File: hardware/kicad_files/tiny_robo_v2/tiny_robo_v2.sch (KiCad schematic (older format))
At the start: 31 parts, among them P2 BATT, P3 CONN_01X02, P4 CONNECTOR, P5 CONNECTOR, P6 CONN_01X02, SW1 SPDT, U1 MCP73831, U2 MIC5265, U3 ESP8266-ESP-03, U4 DRV8830, U5 DRV8830

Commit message: Fixed switch footprint, working on PCB now
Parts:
- Charge1: footprint LEDs:LED-0805 -> LEDs:LED_0805
- P1: renamed from P?; footprint (none) -> Pin_Headers:Pin_Header_Straight_1x06
- R10, R11, R12: renamed from R?; footprint (none) -> Resistors_SMD:R_1206_HandSoldering
- U1, U2: footprint Housings_SOT-23_SOT-143_TSOT-6:SOT-23-5 -> TO_SOT_Packages_SMD:SOT-23-5
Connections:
- net 5Vin: now also P1.4 (P4)
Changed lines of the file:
@@
 $EndComp
 $Comp
-L +3.3V-RESCUE-tiny_robo_v2 #PWR05
+L +3.3V-RESCUE-tiny_robo_v2 #PWR04
 U 1 1 5575F5D2
 P 4500 4800
-F 0 "#PWR05" H 4500 4760 30  0001 C CNN
+F 0 "#PWR04" H 4500 4760 30  0001 C CNN
 F 1 "+3.3V" H 4500 4910 30  0000 C CNN
 F 2 "" H 4500 4800 60  0001 C CNN
@@
 NoConn ~ 7800 1900
 $Comp
-L +BATT #PWR06
+L +BATT #PWR05
 U 1 1 54EFA680
 P 5650 975
-F 0 "#PWR06" H 5650 925 20  0001 C CNN
+F 0 "#PWR05" H 5650 925 20  0001 C CNN
 F 1 "+BATT" H 5650 1075 30  0000 C CNN
 F 2 "" H 5650 975 60  0001 C CNN
@@
 $EndComp
 $Comp
-L +3.3V-RESCUE-tiny_robo_v2 #PWR07
+L +3.3V-RESCUE-tiny_robo_v2 #PWR06
 U 1 1 54EFA66A
 P 8550 1325
-F 0 "#PWR07" H 8550 1285 30  0001 C CNN
+F 0 "#PWR06" H 8550 1285 30  0001 C CNN
 F 1 "+3.3V" H 8550 1435 30  0000 C CNN
 F 2 "" H 8550 1325 60  0001 C CNN
@@
 F 0 "U2" H 7350 2000 60  0000 C CNN
 F 1 "MIC5265" H 7500 1600 60  0000 C CNN
-F 2 "Housings_SOT-23_SOT-143_TSOT-6:SOT-23-5" H 7500 1800 60  0000 C CNN
+F 2 "TO_SOT_Packages_SMD:SOT-23-5" H 7500 1800 60  0000 C CNN
 F 3 "~" H 7500 1800 60  0000 C CNN
 	1    7500 1800
@@
 F 0 "U1" H 4700 2150 60  0000 C CNN
 F 1 "MCP73831" H 4850 1750 60  0000 C CNN
-F 2 "Housings_SOT-23_SOT-143_TSOT-6:SOT-23-5" H 4850 1950 60  0000 C CNN
+F 2 "TO_SOT_Packages_SMD:SOT-23-5" H 4850 1950 60  0000 C CNN
 F 3 "~" H 4850 1950 60  0000 C CNN
 	1    4850 1950
@@
 F 0 "Charge1" H 3650 2150 50  0000 C CNN
 F 1 "LED" H 3650 1950 50  0000 C CNN
-F 2 "LEDs:LED-0805" H 3650 2050 60  0001 C CNN
+F 2 "LEDs:LED_0805" H 3650 2050 60  0001 C CNN
 F 3 "" H 3650 2050 60  0001 C CNN
 	1    3650 2050
@@
 $EndComp
 $Comp
-L GND-RESCUE-tiny_robo_v2 #PWR08
+L GND-RESCUE-tiny_robo_v2 #PWR07
 U 1 1 54EF9ED1
 P 4450 2700
-F 0 "#PWR08" H 4450 2700 30  0001 C CNN
+F 0 "#PWR07" H 4450 2700 30  0001 C CNN
 F 1 "GND" H 4450 2630 30  0001 C CNN
 F 2 "" H 4450 2700 60  0001 C CNN
@@
 	2975 3225 2975 3725
 $Comp
-L GND-RESCUE-tiny_robo_v2 #PWR09
+L GND-RESCUE-tiny_robo_v2 #PWR08
 U 1 1 559D6D0E
 P 2975 3725
-F 0 "#PWR09" H 2975 3725 30  0001 C CNN
+F 0 "#PWR08" H 2975 3725 30  0001 C CNN
 F 1 "GND" H 2975 3655 30  0001 C CNN
 F 2 "" H 2975 3725 60  0000 C CNN
@@
 $EndComp
 $Comp
-L CONN_01X06 P?
+L CONN_01X06 P1
 U 1 1 570E7DDF
 P 2775 5050
-F 0 "P?" H 2775 5400 50  0000 C CNN
+F 0 "P1" H 2775 5400 50  0000 C CNN
 F 1 "CONN_01X06" V 2875 5050 50  0000 C CNN
-F 2 "" H 2775 5050 50  0000 C CNN
+F 2 "Pin_Headers:Pin_Header_Straight_1x06" H 2775 5050 50  0001 C CNN
 F 3 "" H 2775 5050 50  0000 C CNN
 	1    2775 5050
@@
 	3125 4900 2975 4900
 $Comp
-L GND-RESCUE-tiny_robo_v2 #PWR?
+L GND-RESCUE-tiny_robo_v2 #PWR09
 U 1 1 570E86D9
 P 3700 4850
-F 0 "#PWR?" H 3700 4850 30  0001 C CNN
+F 0 "#PWR09" H 3700 4850 30  0001 C CNN
 F 1 "GND-RESCUE-tiny_robo_v2" H 3700 4780 30  0001 C CNN
 F 2 "" H 3700 4850 60  0000 C CNN
@@
 Connection ~ 3700 4800
 $Comp
-L R-RESCUE-tiny_robo_v2 R?
+L R-RESCUE-tiny_robo_v2 R11
 U 1 1 570E8A3E
 P 5125 4425
-F 0 "R?" V 5205 4425 40  0000 C CNN
+F 0 "R11" V 5205 4425 40  0000 C CNN
 F 1 "10k" V 5132 4426 40  0000 C CNN
-F 2 "" V 5055 4425 30  0000 C CNN
+F 2 "Resistors_SMD:R_1206_HandSoldering" V 5055 4425 30  0001 C CNN
 F 3 "" H 5125 4425 30  0000 C CNN
 	1    5125 4425
@@
 $EndComp
 $Comp
-L R-RESCUE-tiny_robo_v2 R?
+L R-RESCUE-tiny_robo_v2 R12
 U 1 1 570E8B63
 P 6125 4475
-F 0 "R?" V 6205 4475 40  0000 C CNN
+F 0 "R12" V 6205 4475 40  0000 C CNN
 F 1 "10k" V 6132 4476 40  0000 C CNN
-F 2 "" V 6055 4475 30  0000 C CNN
+F 2 "Resistors_SMD:R_1206_HandSoldering" V 6055 4475 30  0001 C CNN
 F 3 "" H 6125 4475 30  0000 C CNN
 	1    6125 4475
@@
 	3700 4225 6125 4225
 $Comp
-L R-RESCUE-tiny_robo_v2 R?
+L R-RESCUE-tiny_robo_v2 R10
 U 1 1 57156590
 P 3250 4425
-F 0 "R?" V 3330 4425 40  0000 C CNN
+F 0 "R10" V 3330 4425 40  0000 C CNN
 F 1 "10k" V 3257 4426 40  0000 C CNN
-F 2 "" V 3180 4425 30  0000 C CNN
+F 2 "Resistors_SMD:R_1206_HandSoldering" V 3180 4425 30  0001 C CNN
 F 3 "" H 3250 4425 30  0000 C CNN
 	1    3250 4425
@@
 Wire Wire Line
 	4325 4800 4575 4800
+Wire Wire Line
+	2975 4125 2975 5000
+Text GLabel 2400 4125 0    60   Input ~ 0
+5Vin
+Wire Wire Line
+	2975 4125 2400 4125
 $EndSCHEMATC

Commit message: syncing home version
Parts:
- added C? (x2): 0.1uF, Capacitors_SMD:C_0805_HandSoldering, symbol C-RESCUE-tiny_robo_v2
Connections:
- net GND: now also C?.2, C?.2
- net Unreg: now also C?.1, C?.1
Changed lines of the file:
@@
 EESchema Schematic File Version 2
+LIBS:tiny_robo_v2-rescue
 LIBS:power
 LIBS:device
@@
 	5650 1300 6275 1300
 Wire Wire Line
-	8650 5525 8650 6600
+	8650 5450 8650 6600
 Connection ~ 7850 6600
 Connection ~ 9650 3775
@@
 Wire Wire Line
 	2975 4125 2400 4125
+$Comp
+L C-RESCUE-tiny_robo_v2 C?
+U 1 1 57E440DA
+P 8975 5450
+F 0 "C?" H 9025 5550 50  0000 L CNN
+F 1 "0.1uF" H 9025 5350 50  0000 L CNN
+F 2 "Capacitors_SMD:C_0805_HandSoldering" H 8975 5450 60  0001 C CNN
+F 3 "" H 8975 5450 60  0001 C CNN
+	1    8975 5450
+	0    1    1    0
+$EndComp
+$Comp
+L C-RESCUE-tiny_robo_v2 C?
+U 1 1 57E442F8
+P 8975 5750
+F 0 "C?" H 9025 5850 50  0000 L CNN
+F 1 "0.1uF" H 9025 5650 50  0000 L CNN
+F 2 "Capacitors_SMD:C_0805_HandSoldering" H 8975 5750 60  0001 C CNN
+F 3 "" H 8975 5750 60  0001 C CNN
+	1    8975 5750
+	0    1    1    0
+$EndComp
+Wire Wire Line
+	8775 5450 8650 5450
+Connection ~ 8650 5525
+Wire Wire Line
+	8775 5750 8650 5750
+Connection ~ 8650 5750
+Wire Wire Line
+	8375 6225 8375 6175
+Wire Wire Line
+	8375 6175 8825 6175
+Wire Wire Line
+	8825 6175 8825 5850
+Wire Wire Line
+	8825 5850 9175 5850
+Wire Wire Line
+	9175 5850 9175 5750
+Wire Wire Line
+	8375 5200 8375 5250
+Wire Wire Line
+	8375 5250 9000 5250
+Wire Wire Line
+	9000 5250 9000 5400
+Wire Wire Line
+	9000 5400 9175 5400
+Wire Wire Line
+	9175 5400 9175 5450
 $EndSCHEMATC

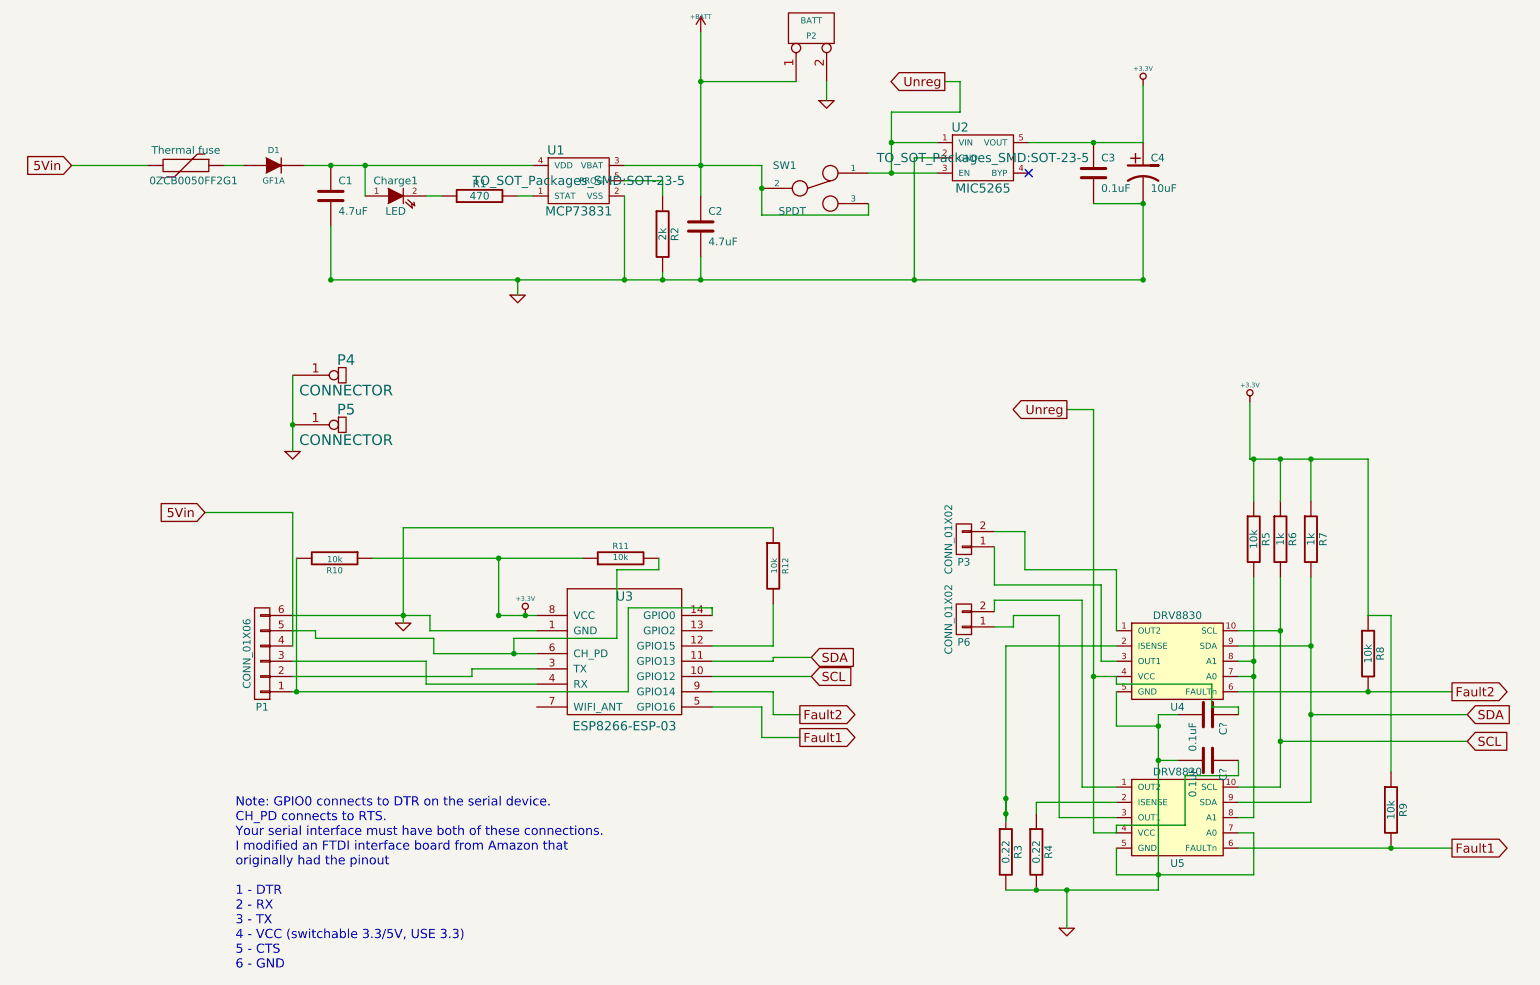
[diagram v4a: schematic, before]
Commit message: Updated schematic, board probably needs relayout (after I graduate).
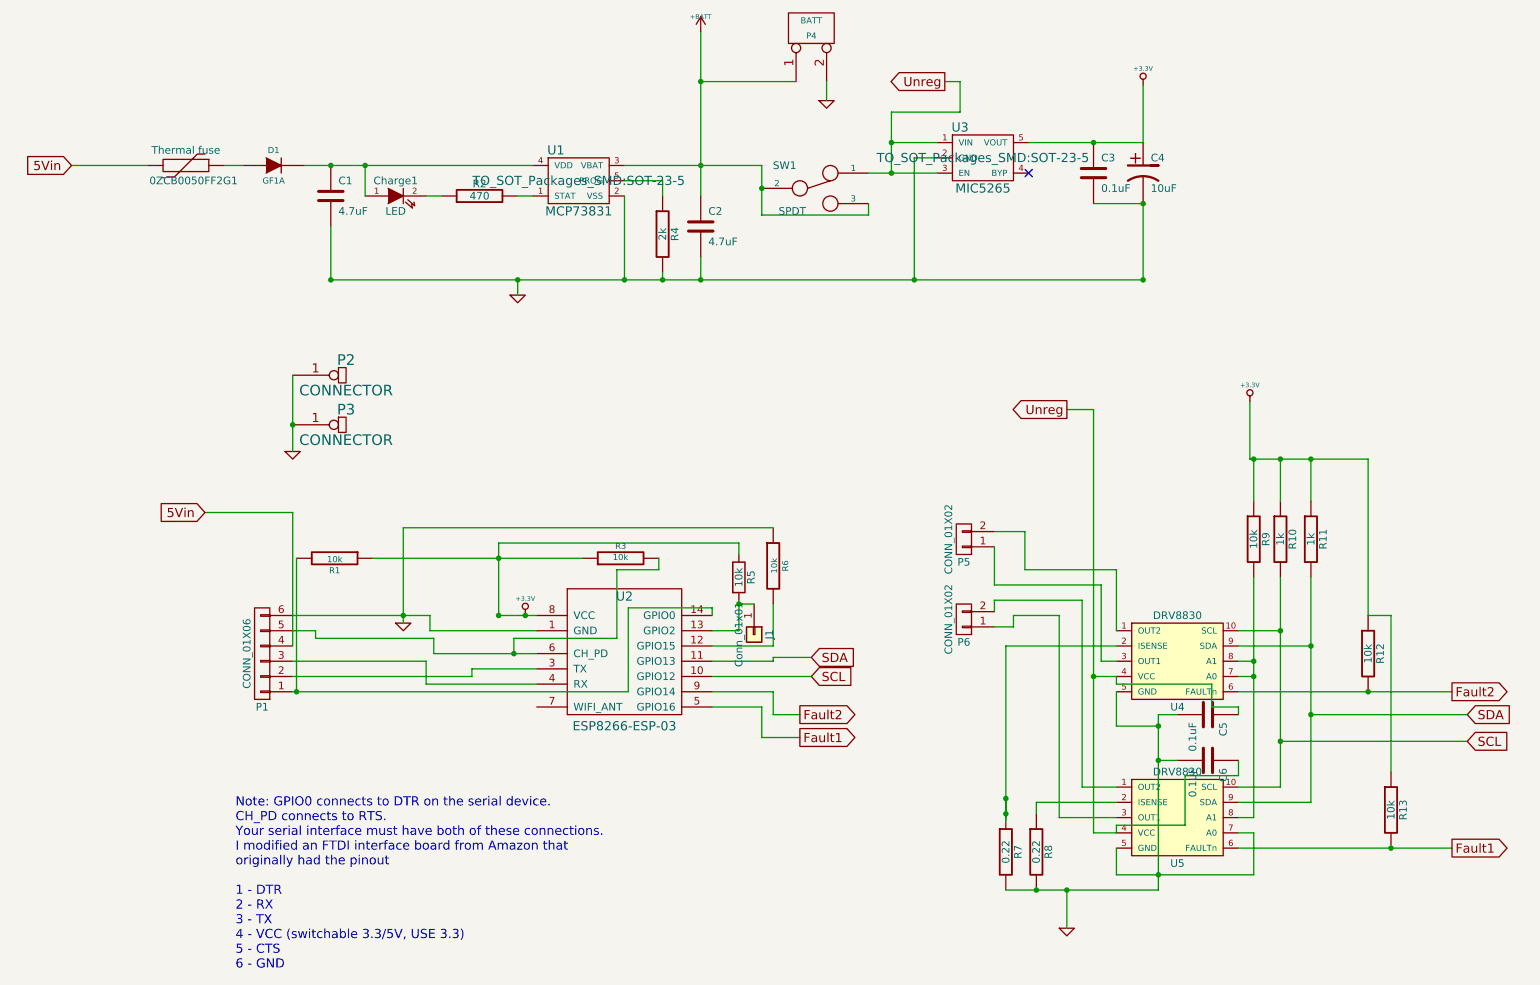
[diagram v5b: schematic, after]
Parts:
- added J1: Conn_01x01, Pin_Headers:Pin_Header_Straight_1x01_Pitch1.00mm, symbol Conn_01x01
- added R5: 10k, Resistors_SMD:R_1206_HandSoldering, symbol R
- gave numbers to parts that had none: 2
- renumbered P4 to P2, P5 to P3, P2 to P4, P3 to P5, R10 to R1, R6 to R10, R7 to R11, R8 to R12, R9 to R13, R1 to R2, R11 to R3, R2 to R4, R12 to R6, R3 to R7, R4 to R8, R5 to R9, U3 to U2, U2 to U3
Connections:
- net +3.3V: now also R5.1
- net at U2.13 (GPIO2): now also J1.1 (Pin_1), R5.2
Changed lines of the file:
@@
 EESchema Schematic File Version 2
-LIBS:tiny_robo_v2-rescue
 LIBS:power
 LIBS:device
@@
 $EndComp
 $Comp
-L R-RESCUE-tiny_robo_v2 R5
+L R-RESCUE-tiny_robo_v2 R9
 U 1 1 5576FFFF
 P 9275 4300
-F 0 "R5" V 9355 4300 50  0000 C CNN
+F 0 "R9" V 9355 4300 50  0000 C CNN
 F 1 "10k" V 9275 4300 50  0000 C CNN
 F 2 "Resistors_SMD:R_1206_HandSoldering" H 9275 4300 60  0001 C CNN
@@
 $EndComp
 $Comp
-L R-RESCUE-tiny_robo_v2 R8
+L R-RESCUE-tiny_robo_v2 R12
 U 1 1 5576FE5F
 P 10025 5050
-F 0 "R8" V 10105 5050 50  0000 C CNN
+F 0 "R12" V 10105 5050 50  0000 C CNN
 F 1 "10k" V 10025 5050 50  0000 C CNN
 F 2 "Resistors_SMD:R_1206_HandSoldering" H 10025 5050 60  0001 C CNN
@@
 $EndComp
 $Comp
-L R-RESCUE-tiny_robo_v2 R9
+L R-RESCUE-tiny_robo_v2 R13
 U 1 1 5576FE58
 P 10175 6075
-F 0 "R9" V 10255 6075 50  0000 C CNN
+F 0 "R13" V 10255 6075 50  0000 C CNN
 F 1 "10k" V 10175 6075 50  0000 C CNN
 F 2 "Resistors_SMD:R_1206_HandSoldering" H 10175 6075 60  0001 C CNN
@@
 $EndComp
 $Comp
-L R-RESCUE-tiny_robo_v2 R7
+L R-RESCUE-tiny_robo_v2 R11
 U 1 1 5576FE2F
 P 9650 4300
-F 0 "R7" V 9730 4300 50  0000 C CNN
+F 0 "R11" V 9730 4300 50  0000 C CNN
 F 1 "1k" V 9650 4300 50  0000 C CNN
 F 2 "Resistors_SMD:R_1206_HandSoldering" H 9650 4300 60  0001 C CNN
@@
 $EndComp
 $Comp
-L R-RESCUE-tiny_robo_v2 R6
+L R-RESCUE-tiny_robo_v2 R10
 U 1 1 5576FE2B
 P 9450 4300
-F 0 "R6" V 9530 4300 50  0000 C CNN
+F 0 "R10" V 9530 4300 50  0000 C CNN
 F 1 "1k" V 9450 4300 50  0000 C CNN
 F 2 "Resistors_SMD:R_1206_HandSoldering" H 9450 4300 60  0001 C CNN
@@
 $EndComp
 $Comp
-L R-RESCUE-tiny_robo_v2 R4
+L R-RESCUE-tiny_robo_v2 R8
 U 1 1 5576FE28
 P 7850 6350
-F 0 "R4" V 7930 6350 50  0000 C CNN
+F 0 "R8" V 7930 6350 50  0000 C CNN
 F 1 "0.22" V 7850 6350 50  0000 C CNN
 F 2 "Resistors_SMD:R_1206_HandSoldering" H 7850 6350 60  0001 C CNN
@@
 $EndComp
 $Comp
-L R-RESCUE-tiny_robo_v2 R3
+L R-RESCUE-tiny_robo_v2 R7
 U 1 1 5576FE1B
 P 7650 6350
-F 0 "R3" V 7730 6350 50  0000 C CNN
+F 0 "R7" V 7730 6350 50  0000 C CNN
 F 1 "0.22" V 7650 6350 50  0000 C CNN
 F 2 "Resistors_SMD:R_1206_HandSoldering" H 7650 6350 60  0001 C CNN
@@
 $EndComp
 $Comp
-L CONN_2 P2
+L CONN_2 P4
 U 1 1 54EFA433
 P 6375 950
-F 0 "P2" V 6325 950 40  0000 C CNN
+F 0 "P4" V 6325 950 40  0000 C CNN
 F 1 "BATT" V 6425 950 40  0000 C CNN
 F 2 "Pin_Headers:Pin_Header_Straight_1x02" H 6375 950 60  0001 C CNN
@@
 $EndComp
 $Comp
-L MIC5265 U2
+L MIC5265 U3
 U 1 1 54EFA34D
 P 7500 1800
-F 0 "U2" H 7350 2000 60  0000 C CNN
+F 0 "U3" H 7350 2000 60  0000 C CNN
 F 1 "MIC5265" H 7500 1600 60  0000 C CNN
 F 2 "TO_SOT_Packages_SMD:SOT-23-5" H 7500 1800 60  0000 C CNN
@@
 $EndComp
 $Comp
-L R-RESCUE-tiny_robo_v2 R1
+L R-RESCUE-tiny_robo_v2 R2
 U 1 1 54EF9F5C
 P 4200 2050
-F 0 "R1" V 4280 2050 50  0000 C CNN
+F 0 "R2" V 4280 2050 50  0000 C CNN
 F 1 "470" V 4200 2050 50  0000 C CNN
 F 2 "Resistors_SMD:R_1206_HandSoldering" H 4200 2050 60  0001 C CNN
@@
 $EndComp
 $Comp
-L R-RESCUE-tiny_robo_v2 R2
+L R-RESCUE-tiny_robo_v2 R4
 U 1 1 54EF9F56
 P 5400 2300
-F 0 "R2" V 5480 2300 50  0000 C CNN
+F 0 "R4" V 5480 2300 50  0000 C CNN
 F 1 "2k" V 5400 2300 50  0000 C CNN
 F 2 "Resistors_SMD:R_1206_HandSoldering" H 5400 2300 60  0001 C CNN
@@
 	9175 5300 10575 5300
 $Comp
-L CONNECTOR P4
+L CONNECTOR P2
 U 1 1 559D6607
 P 2975 3225
-F 0 "P4" H 3325 3325 70  0000 C CNN
+F 0 "P2" H 3325 3325 70  0000 C CNN
 F 1 "CONNECTOR" H 3325 3125 70  0000 C CNN
 F 2 "Wire_Pads:SolderWirePad_single_0-8mmDrill" H 2975 3225 60  0001 C CNN
@@
 $EndComp
 $Comp
-L CONNECTOR P5
+L CONNECTOR P3
 U 1 1 559D66C8
 P 2975 3550
-F 0 "P5" H 3325 3650 70  0000 C CNN
+F 0 "P3" H 3325 3650 70  0000 C CNN
 F 1 "CONNECTOR" H 3325 3450 70  0000 C CNN
 F 2 "Wire_Pads:SolderWirePad_single_0-8mmDrill" H 2975 3550 60  0001 C CNN
@@
 Connection ~ 2975 3550
 $Comp
-L CONN_01X02 P3
+L CONN_01X02 P5
 U 1 1 559D733F
 P 7375 4300
-F 0 "P3" H 7375 4450 50  0000 C CNN
+F 0 "P5" H 7375 4450 50  0000 C CNN
 F 1 "CONN_01X02" V 7475 4300 50  0000 C CNN
 F 2 "Pin_Headers:Pin_Header_Straight_1x02" H 7375 4300 60  0001 C CNN
@@
 	6050 5600 6300 5600
 $Comp
-L ESP8266-ESP-03 U3
+L ESP8266-ESP-03 U2
 U 1 1 5575F418
 P 5150 5400
-F 0 "U3" H 5150 6125 60  0000 C CNN
+F 0 "U2" H 5150 6125 60  0000 C CNN
 F 1 "ESP8266-ESP-03" H 5150 5275 60  0000 C CNN
 F 2 "esp-8266:ESP8266-ESP-03" H 5150 5400 60  0001 C CNN
@@
 Connection ~ 3700 4800
 $Comp
-L R-RESCUE-tiny_robo_v2 R11
+L R-RESCUE-tiny_robo_v2 R3
 U 1 1 570E8A3E
 P 5125 4425
-F 0 "R11" V 5205 4425 40  0000 C CNN
+F 0 "R3" V 5205 4425 40  0000 C CNN
 F 1 "10k" V 5132 4426 40  0000 C CNN
 F 2 "Resistors_SMD:R_1206_HandSoldering" V 5055 4425 30  0001 C CNN
@@
 $EndComp
 $Comp
-L R-RESCUE-tiny_robo_v2 R12
+L R-RESCUE-tiny_robo_v2 R6
 U 1 1 570E8B63
 P 6125 4475
-F 0 "R12" V 6205 4475 40  0000 C CNN
+F 0 "R6" V 6205 4475 40  0000 C CNN
 F 1 "10k" V 6132 4476 40  0000 C CNN
 F 2 "Resistors_SMD:R_1206_HandSoldering" V 6055 4475 30  0001 C CNN
@@
 	3500 4425 4875 4425
 Wire Wire Line
-	4325 4425 4325 4800
+	4325 4325 4325 4800
 Connection ~ 4325 4800
 Wire Wire Line
 	3700 4225 6125 4225
 $Comp
-L R-RESCUE-tiny_robo_v2 R10
+L R-RESCUE-tiny_robo_v2 R1
 U 1 1 57156590
 P 3250 4425
-F 0 "R10" V 3330 4425 40  0000 C CNN
+F 0 "R1" V 3330 4425 40  0000 C CNN
 F 1 "10k" V 3257 4426 40  0000 C CNN
 F 2 "Resistors_SMD:R_1206_HandSoldering" V 3180 4425 30  0001 C CNN
@@
 	2975 4125 2400 4125
 $Comp
-L C-RESCUE-tiny_robo_v2 C?
+L C-RESCUE-tiny_robo_v2 C5
 U 1 1 57E440DA
 P 8975 5450
-F 0 "C?" H 9025 5550 50  0000 L CNN
+F 0 "C5" H 9025 5550 50  0000 L CNN
 F 1 "0.1uF" H 9025 5350 50  0000 L CNN
 F 2 "Capacitors_SMD:C_0805_HandSoldering" H 8975 5450 60  0001 C CNN
@@
 $EndComp
 $Comp
-L C-RESCUE-tiny_robo_v2 C?
+L C-RESCUE-tiny_robo_v2 C6
 U 1 1 57E442F8
 P 8975 5750
-F 0 "C?" H 9025 5850 50  0000 L CNN
+F 0 "C6" H 9025 5850 50  0000 L CNN
 F 1 "0.1uF" H 9025 5650 50  0000 L CNN
 F 2 "Capacitors_SMD:C_0805_HandSoldering" H 8975 5750 60  0001 C CNN
@@
 Wire Wire Line
 	9175 5400 9175 5450
+$Comp
+L R R5
+U 1 1 5BCF6F13
+P 5900 4550
+F 0 "R5" V 5980 4550 50  0000 C CNN
+F 1 "10k" V 5900 4550 50  0000 C CNN
+F 2 "Resistors_SMD:R_1206_HandSoldering" V 5830 4550 50  0001 C CNN
+F 3 "" H 5900 4550 50  0001 C CNN
+	1    5900 4550
+	1    0    0    -1
+$EndComp
+Wire Wire Line
+	5725 4900 5900 4900
+Wire Wire Line
+	5900 4900 5900 4700
+Wire Wire Line
+	4325 4325 5900 4325
+Wire Wire Line
+	5900 4325 5900 4400
+$Comp
+L Conn_01x01 J1
+U 1 1 5BCF7ECC
+P 6000 4925
+F 0 "J1" H 6000 5025 50  0000 C CNN
+F 1 "Conn_01x01" H 6000 4825 50  0000 C CNN
+F 2 "Pin_Headers:Pin_Header_Straight_1x01_Pitch1.00mm" H 6000 4925 50  0001 C CNN
+F 3 "" H 6000 4925 50  0001 C CNN
+	1    6000 4925
+	0    1    1    0
+$EndComp
+Wire Wire Line
+	6000 4725 5900 4725
+Connection ~ 5900 4725
 $EndSCHEMATC
